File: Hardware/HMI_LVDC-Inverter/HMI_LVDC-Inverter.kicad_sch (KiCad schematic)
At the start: 10 parts, among them J1 Micro_PwrBus_B1, J10 Inv_Signal2_A1, J2 Screw_Terminal_01x07, J3 START_BTN1, J4 TERMO_SW1, J5 STOP_BTN1, J6 SWD_Program1, J7 Inverter_MEAS, J8 Inv_Signal1_A1, J9 ESP32_Programmer

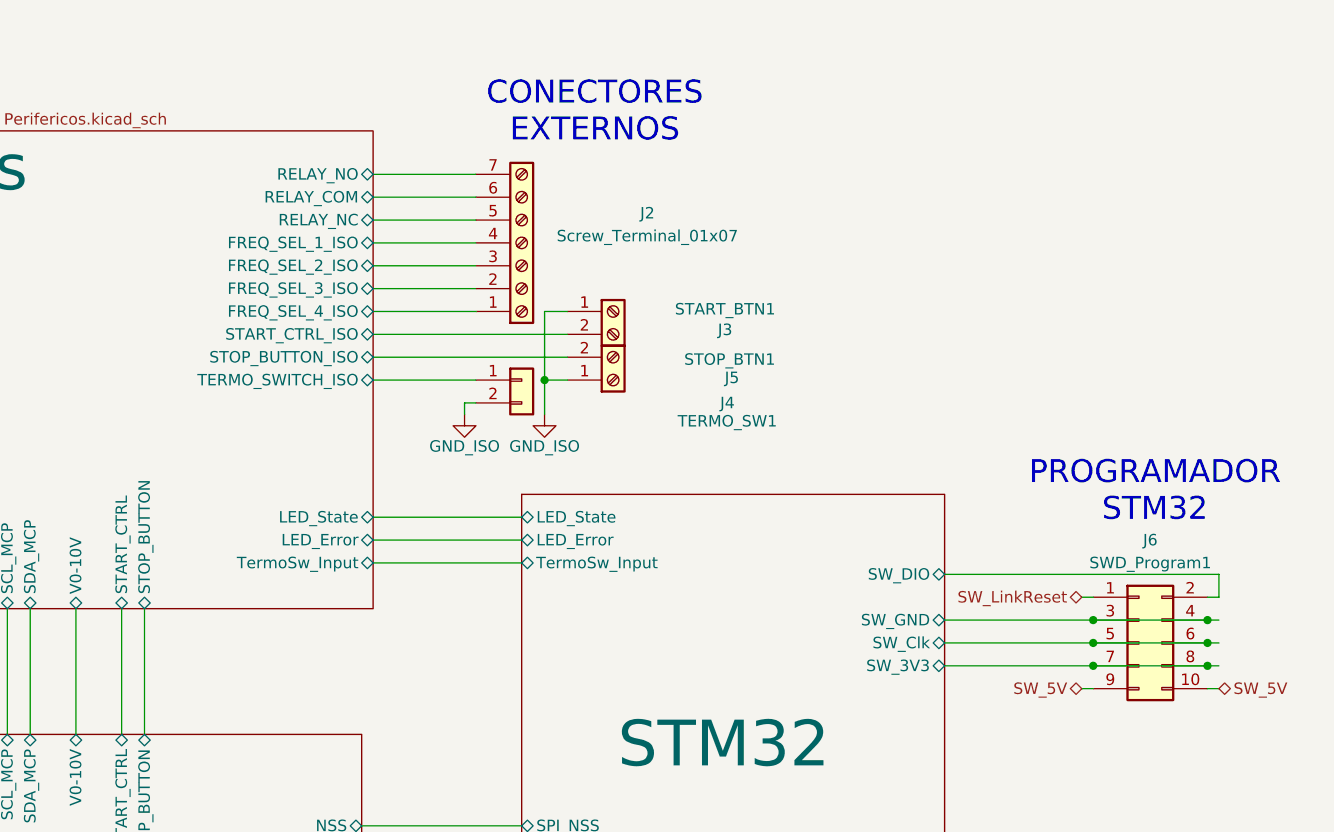
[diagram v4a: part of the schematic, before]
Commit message: Avances en el PCB, arreglos en el esquema y agregado de borneras de gabinete
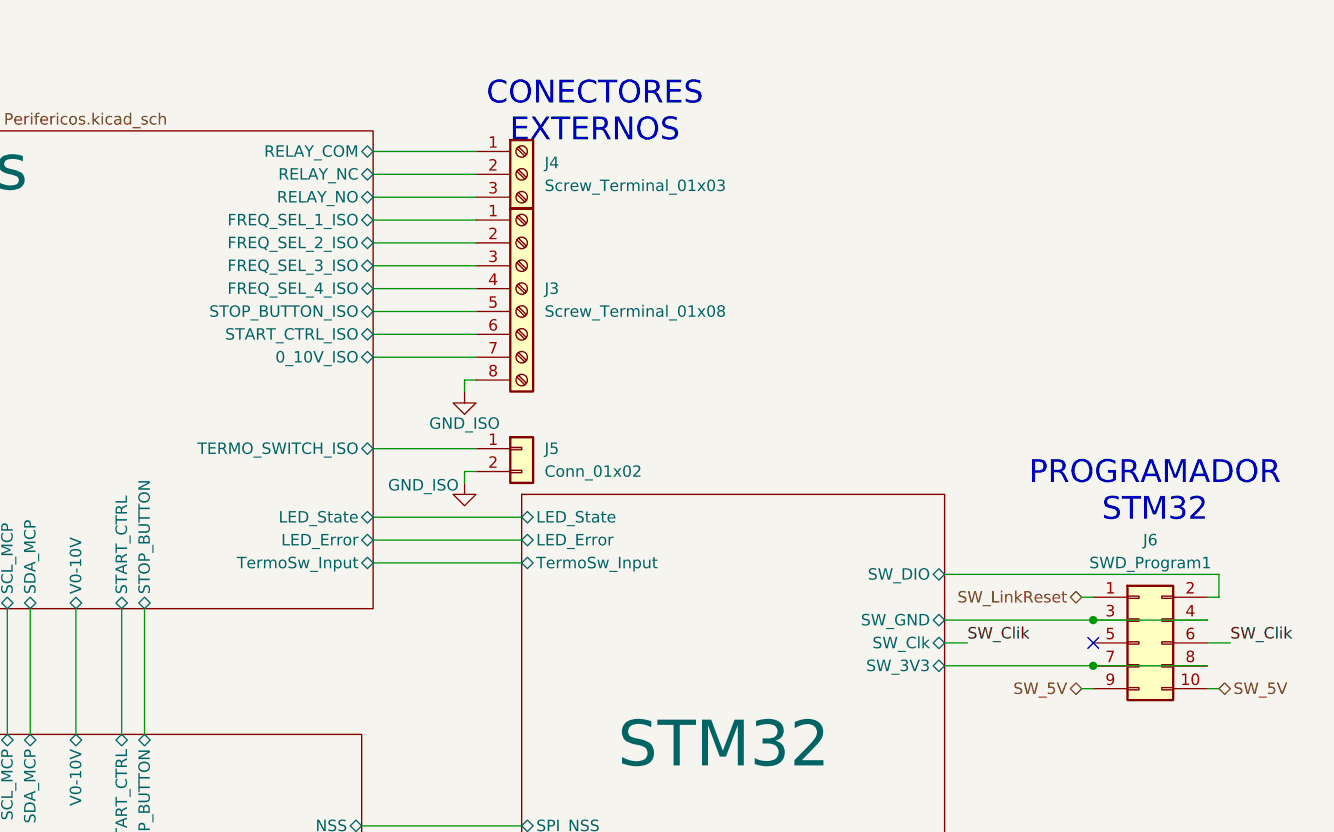
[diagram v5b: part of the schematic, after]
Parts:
- removed J2: Screw_Terminal_01x07, TerminalBlock_Phoenix:TerminalBlock_Phoenix_PT-1,5-7-5.0-H_1x07_P5.00mm_Horizontal, symbol Connector:Screw_Terminal_01x07
- removed J3: START_BTN1, TerminalBlock_Phoenix:TerminalBlock_Phoenix_MKDS-1,5-2_1x02_P5.00mm_Horizontal, symbol Connector:Screw_Terminal_01x02
- removed J4: TERMO_SW1, Connector_Molex:Molex_KK-254_AE-6410-02A_1x02_P2.54mm_Vertical, symbol Connector_Generic:Conn_01x02
- removed J5: STOP_BTN1, TerminalBlock_Phoenix:TerminalBlock_Phoenix_MKDS-1,5-2_1x02_P5.00mm_Horizontal, symbol Connector:Screw_Terminal_01x02
- added J3: Screw_Terminal_01x08, Footprints:MX250-3.5-08P-B-GY01-Cu-A, symbol Connector:Screw_Terminal_01x08
- added J4: Screw_Terminal_01x03, Footprints:MX250-3.5-03P-A-GY01-Cu-A, symbol Connector:Screw_Terminal_01x03
- added J5: Conn_01x02, Connector_Molex:Molex_KK-254_AE-6410-02A_1x02_P2.54mm_Vertical, symbol Connector_Generic:Conn_01x02
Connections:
- net GND_ISO: now also J3.8 (Pin_8), J5.2 (Pin_2)
- net Perifericos/FREQ_SEL_1_ISO: now also J3.1 (Pin_1)
- net Perifericos/FREQ_SEL_2_ISO: now also J3.2 (Pin_2)
- net Perifericos/FREQ_SEL_3_ISO: now also J3.3 (Pin_3)
- net Perifericos/FREQ_SEL_4_ISO: now also J3.4 (Pin_4)
- net Perifericos/RELAY_COM: now also J4.1 (Pin_1)
- net Perifericos/RELAY_NC: now also J4.2 (Pin_2)
- net Perifericos/RELAY_NO: now also J4.3 (Pin_3)
- net Perifericos/START_CTRL_ISO: now also J3.6 (Pin_6)
- net Perifericos/STOP_BUTTON_ISO: now also J3.5 (Pin_5)
- net Perifericos/TERMO_SWITCH_ISO: now also J5.1 (Pin_1)
- net STM32/SW_Clk: no longer names the net of J6.5 (Pin_5)
- net STM32/SW_Clk: no longer J6.6 (Pin_6)
- new net Perifericos/0_10V_ISO: J3.7 (Pin_7)
- new net SW_Clik: J6.6 (Pin_6)
- no-connect marks 0 -> 1
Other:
- sheet Perifericos ports: added 0_10V_ISO; removed none

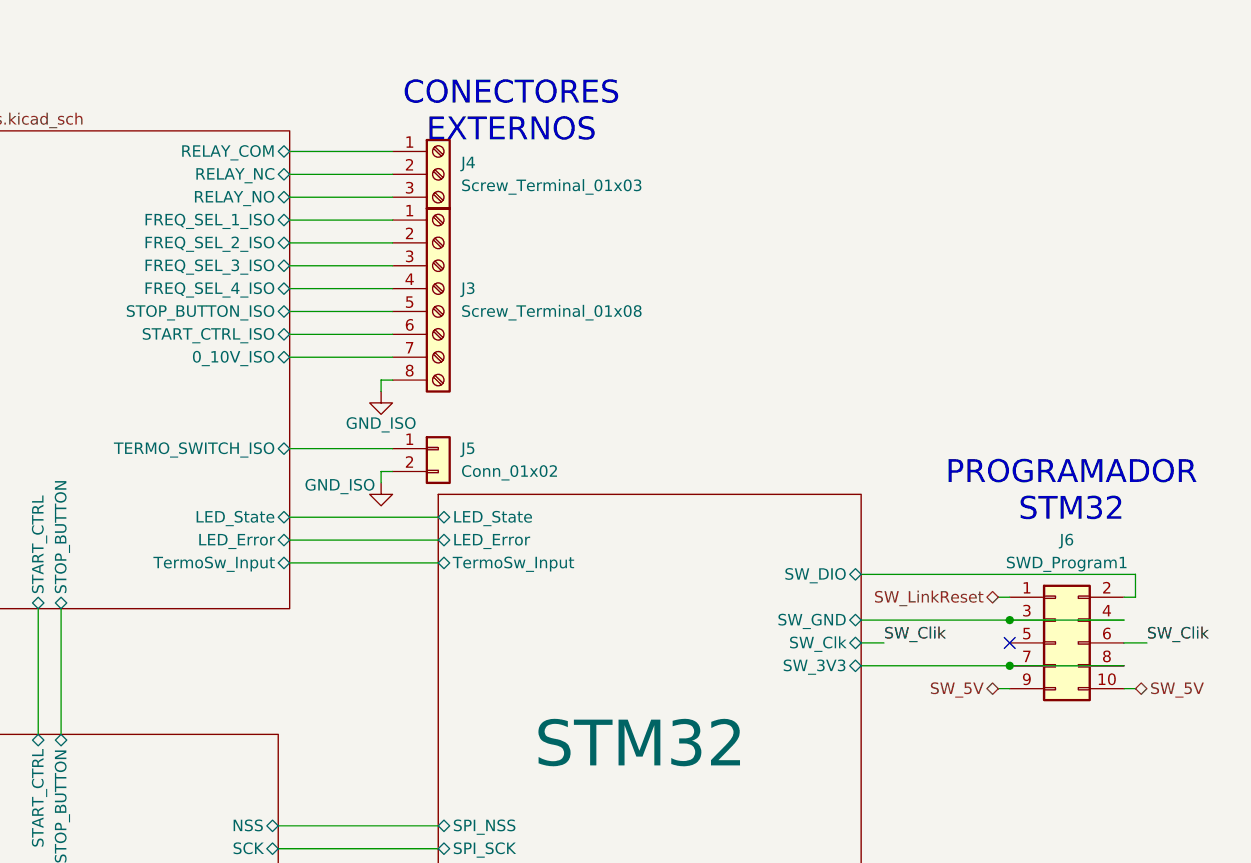
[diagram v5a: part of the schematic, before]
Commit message: Falta resolver los pulsadores
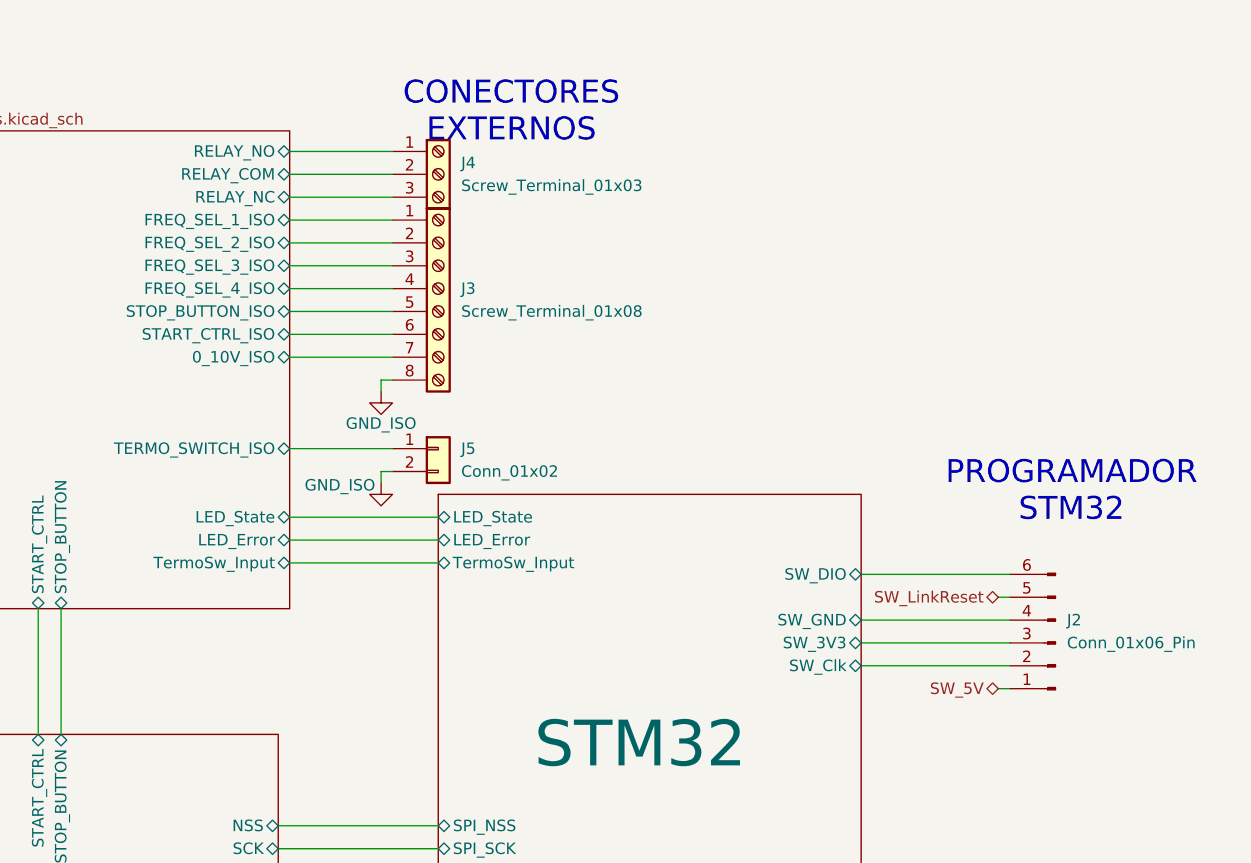
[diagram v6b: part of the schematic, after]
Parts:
- removed J6: SWD_Program1, Connector_IDC:IDC-Header_2x05_P2.54mm_Vertical_SMD, symbol Connector_Generic:Conn_02x05_Odd_Even
- added J2: Conn_01x06_Pin, Connector_PinHeader_1.00mm:PinHeader_1x06_P1.00mm_Vertical, symbol Connector:Conn_01x06_Pin
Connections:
- net Perifericos/RELAY_COM: now also J4.2 (Pin_2); no longer J4.1 (Pin_1)
- net Perifericos/RELAY_NC: now also J4.3 (Pin_3); no longer J4.2 (Pin_2)
- net Perifericos/RELAY_NO: now also J4.1 (Pin_1); no longer J4.3 (Pin_3)
- net STM32/SW_3V3: now also J2.3 (Pin_3)
- net STM32/SW_DIO: now also J2.6 (Pin_6)
- net STM32/SW_GND: now also J2.4 (Pin_4)
- net SW_5V: now also J2.1 (Pin_1)
- net SW_LinkReset: now also J2.5 (Pin_5)
- new net STM32/SW_Clk: J2.2 (Pin_2)
- no-connect marks 1 -> 0

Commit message: Agregado y corrección de borneras
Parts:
- removed J10: Inv_Signal2_A1, Connector_Molex:Molex_KK-254_AE-6410-04A_1x04_P2.54mm_Vertical, symbol Connector_Generic:Conn_01x04
- removed J2: Conn_01x06_Pin, Connector_PinHeader_1.00mm:PinHeader_1x06_P1.00mm_Vertical, symbol Connector:Conn_01x06_Pin
- added J11: STM32_Programmer, Connector_PinHeader_2.54mm:PinHeader_1x06_P2.54mm_Vertical, symbol Connector_Generic:Conn_01x06
- added J9: Conn_01x06, Connector_JST:JST_XH_B6B-XH-A_1x06_P2.50mm_Vertical, symbol Connector_Generic:Conn_01x06
- J1: footprint Connector_Phoenix_MSTB:PhoenixContact_MSTBVA_2,5_2-G-5,08_1x02_P5.08mm_Vertical -> Connector_JST:JST_XH_B3B-XH-A_1x03_P2.50mm_Vertical; symbol Connector_Generic:Conn_01x02 -> Connector_Generic:Conn_01x03; Compra (none) -> https://www.lcsc.com/product-detail/C22388695.html?s_z=n_ZX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; Footprint checked (none) -> Yes; Manufacturer (none) -> Megastar; Price (none) -> 0.0247; Symbol checked (none) -> Yes
- J2: renamed from J4; Compra (none) -> https://www.lcsc.com/product-detail/C7470117.html?s_z=n_MX2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; Footprint checked (none) -> Yes; Manufacturer (none) -> MAX; Price (none) -> 0.1426; Symbol checked (none) -> Yes
- J3: Compra (none) -> https://www.lcsc.com/product-detail/C7467034.html?s_z=n_MX2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; Footprint checked (none) -> Yes; Manufacturer (none) -> MAX; Price (none) -> 0.3497; Symbol checked (none) -> Yes
- J4: renamed from J5; footprint Connector_Molex:Molex_KK-254_AE-6410-02A_1x02_P2.54mm_Vertical -> Connector_JST:JST_EH_B2B-EH-A_1x02_P2.50mm_Vertical; Compra (none) -> https://www.lcsc.com/product-detail/C7429614.html?s_z=n_ZX-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; Footprint checked (none) -> Yes; Manufacturer (none) -> Megastar; Price (none) -> 0.0117; Symbol checked (none) -> Yes
- J6: renamed from J7; footprint Connector_PinHeader_1.00mm:PinHeader_1x05_P1.00mm_Vertical -> Connector_JST:JST_XH_B5B-XH-A_1x05_P2.50mm_Vertical; Compra (none) -> https://www.lcsc.com/product-detail/C7429617.html?s_z=n_ZX-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; Footprint checked (none) -> Yes; Manufacturer (none) -> Megastar; Price (none) -> 0.0278; Symbol checked (none) -> Yes
- J7: renamed from J8; footprint Connector_Molex:Molex_KK-254_AE-6410-04A_1x04_P2.54mm_Vertical -> Connector_JST:JST_XH_B4B-XH-A_1x04_P2.50mm_Vertical; Compra (none) -> https://www.lcsc.com/product-detail/C7429616.html?s_z=n_ZX-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; Footprint checked (none) -> Yes; Manufacturer (none) -> Megastar; Price (none) -> 0.0234; Symbol checked (none) -> Yes
- J8: renamed from J9; Compra (none) -> https://www.lcsc.com/product-detail/C492404.html?s_z=n_%252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; Footprint checked (none) -> Yes; Manufacturer (none) -> XFCN; Price (none) -> 0.0283; Symbol checked (none) -> Yes
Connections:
- net +12V_ISO: now also J1.2 (Pin_2); no longer J1.1 (Pin_1)
- net GND: now also J9.1 (Pin_1), J9.4 (Pin_4), J9.6 (Pin_6)
- net GND_ISO: now also J1.1 (Pin_1), J1.3 (Pin_3); no longer J1.2 (Pin_2)
- net STM32/SW_3V3: now also J11.4 (Pin_4)
- net STM32/SW_Clk: now also J11.5 (Pin_5)
- net STM32/SW_DIO: now also J11.1 (Pin_1)
- net STM32/SW_GND: now also J11.3 (Pin_3)
- net STM32/V_Sd: now also J9.2 (Pin_2)
- net STM32/W_In: now also J9.3 (Pin_3)
- net STM32/W_Sd: now also J9.5 (Pin_5)
- net SW_5V: now also J11.6 (Pin_6)
- net SW_LinkReset: now also J11.2 (Pin_2)

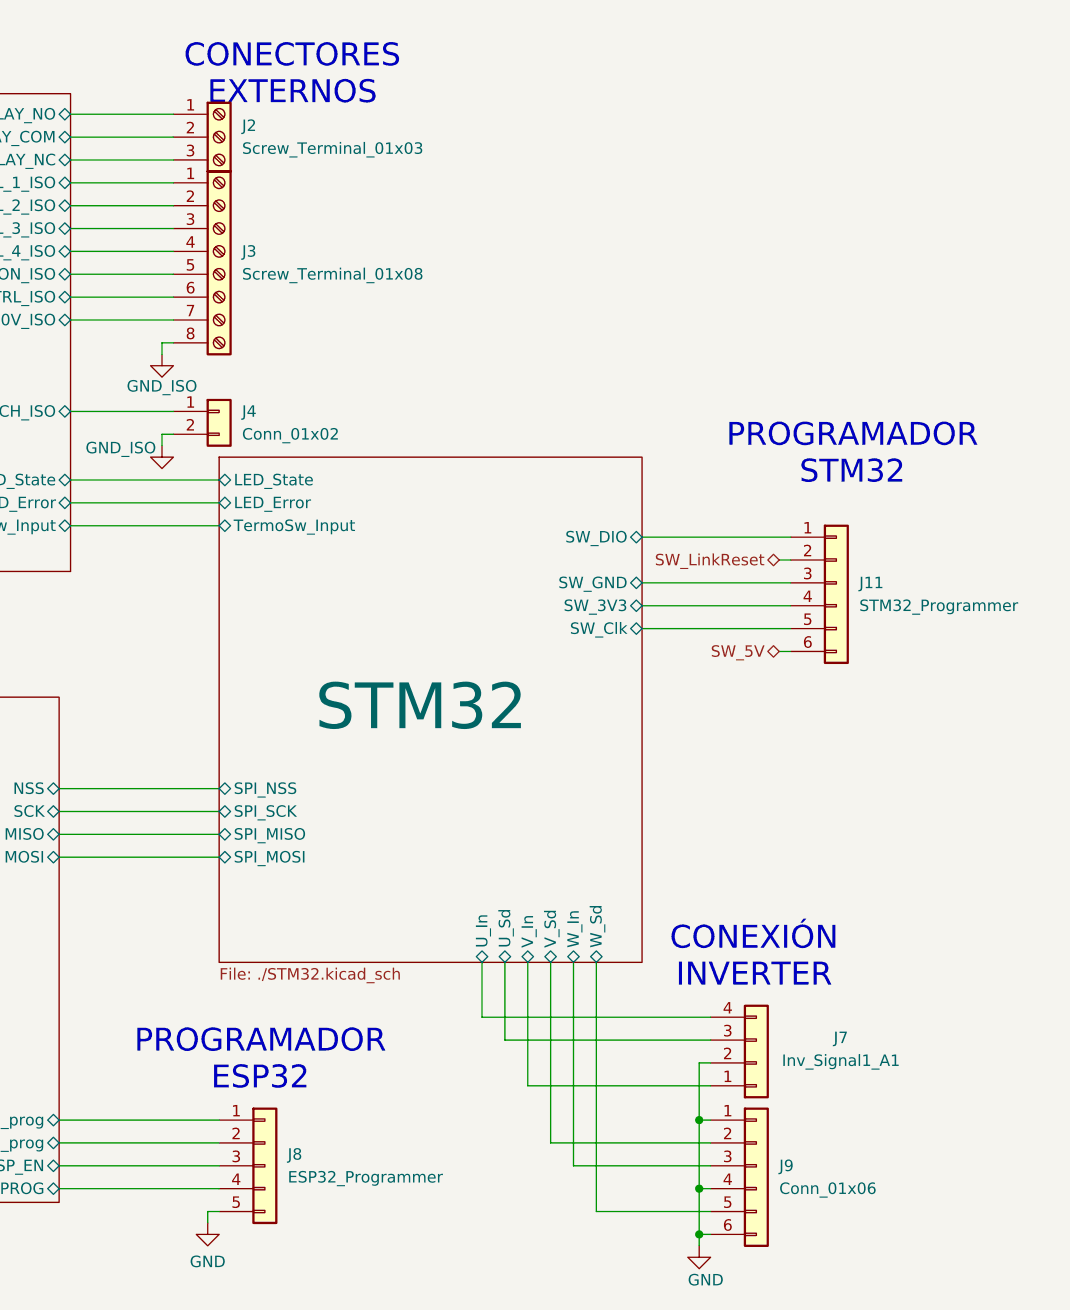
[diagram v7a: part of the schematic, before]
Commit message: Terminada la placa del HMI con revisión de reglas de diseño
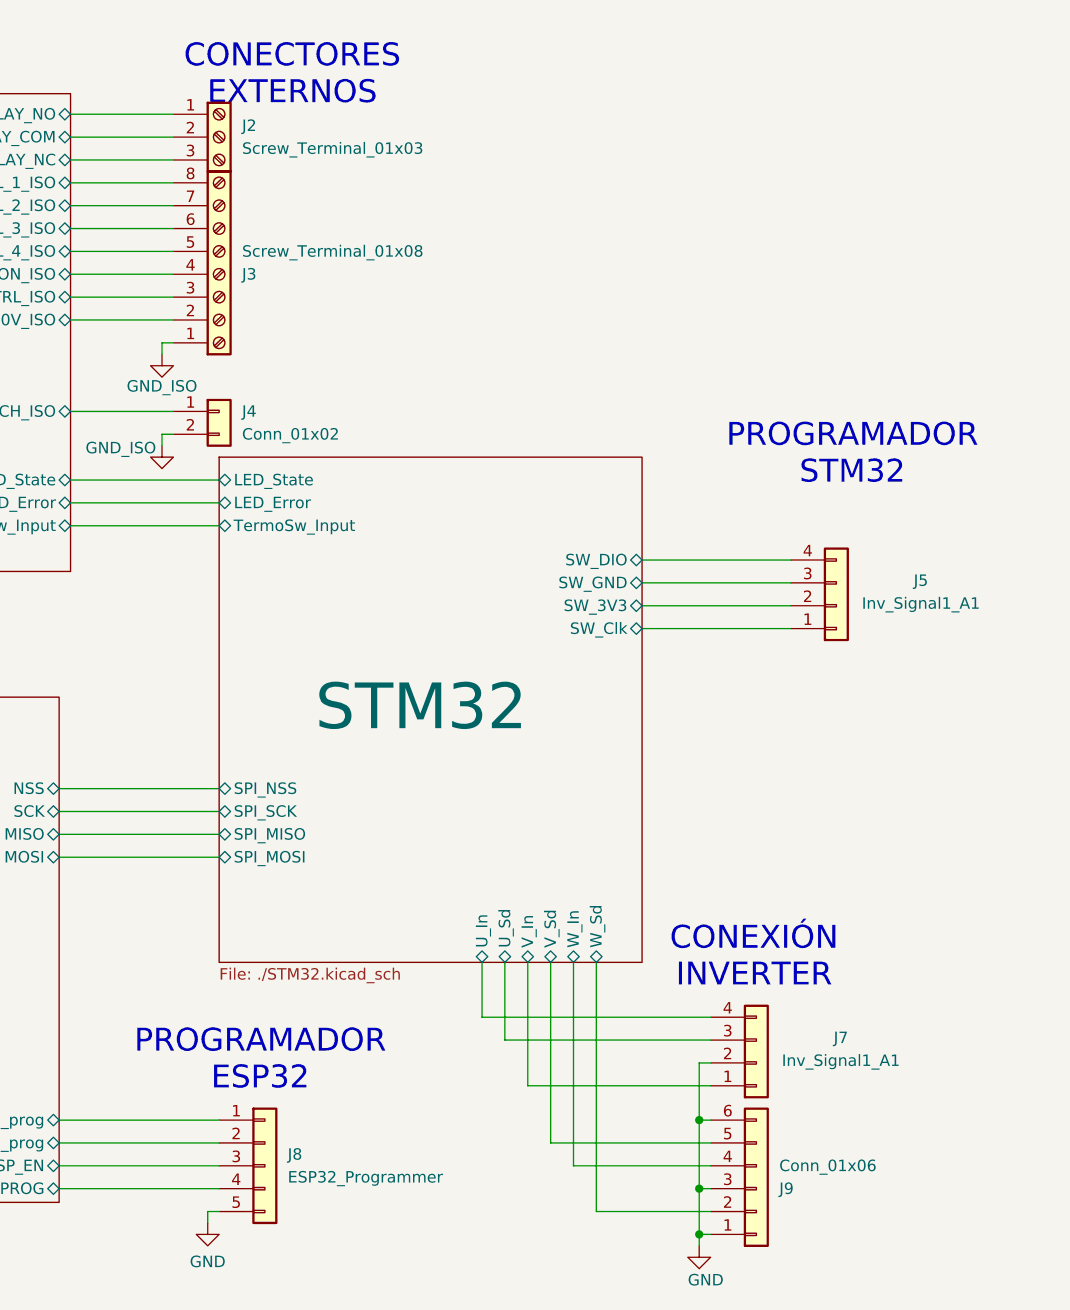
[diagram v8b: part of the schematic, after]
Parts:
- removed J11: STM32_Programmer, Connector_PinHeader_2.54mm:PinHeader_1x06_P2.54mm_Vertical, symbol Connector_Generic:Conn_01x06
- added J5: Inv_Signal1_A1, Connector_PinHeader_2.54mm:PinHeader_1x04_P2.54mm_Vertical, symbol Connector_Generic:Conn_01x04
- J8: footprint Connector_PinHeader_1.00mm:PinHeader_1x05_P1.00mm_Vertical -> Connector_PinHeader_2.54mm:PinHeader_1x05_P2.54mm_Vertical
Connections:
- net GND: now also J9.3 (Pin_3); no longer J9.4 (Pin_4)
- net GND_ISO: now also J3.1 (Pin_1); no longer J3.8 (Pin_8)
- net Perifericos/0_10V_ISO: now also J3.2 (Pin_2); no longer J3.7 (Pin_7)
- net Perifericos/FREQ_SEL_1_ISO: now also J3.8 (Pin_8); no longer J3.1 (Pin_1)
- net Perifericos/FREQ_SEL_2_ISO: now also J3.7 (Pin_7); no longer J3.2 (Pin_2)
- net Perifericos/FREQ_SEL_3_ISO: now also J3.6 (Pin_6); no longer J3.3 (Pin_3)
- net Perifericos/FREQ_SEL_4_ISO: now also J3.5 (Pin_5); no longer J3.4 (Pin_4)
- net Perifericos/START_CTRL_ISO: now also J3.3 (Pin_3); no longer J3.6 (Pin_6)
- net Perifericos/STOP_BUTTON_ISO: now also J3.4 (Pin_4); no longer J3.5 (Pin_5)
- net STM32/SW_3V3: now also J5.2 (Pin_2)
- net STM32/SW_Clk: now also J5.1 (Pin_1)
- net STM32/SW_DIO: now also J5.4 (Pin_4)
- net STM32/SW_GND: now also J5.3 (Pin_3)
- net STM32/V_Sd: now also J9.5 (Pin_5); no longer J9.2 (Pin_2)
- net STM32/W_In: now also J9.4 (Pin_4); no longer J9.3 (Pin_3)
- net STM32/W_Sd: now also J9.2 (Pin_2); no longer J9.5 (Pin_5)
